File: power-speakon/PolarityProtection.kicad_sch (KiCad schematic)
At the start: 7 parts, among them Q201 BSC010N04LS, Q202 BSC010N04LS, U201 LM74502-Q1

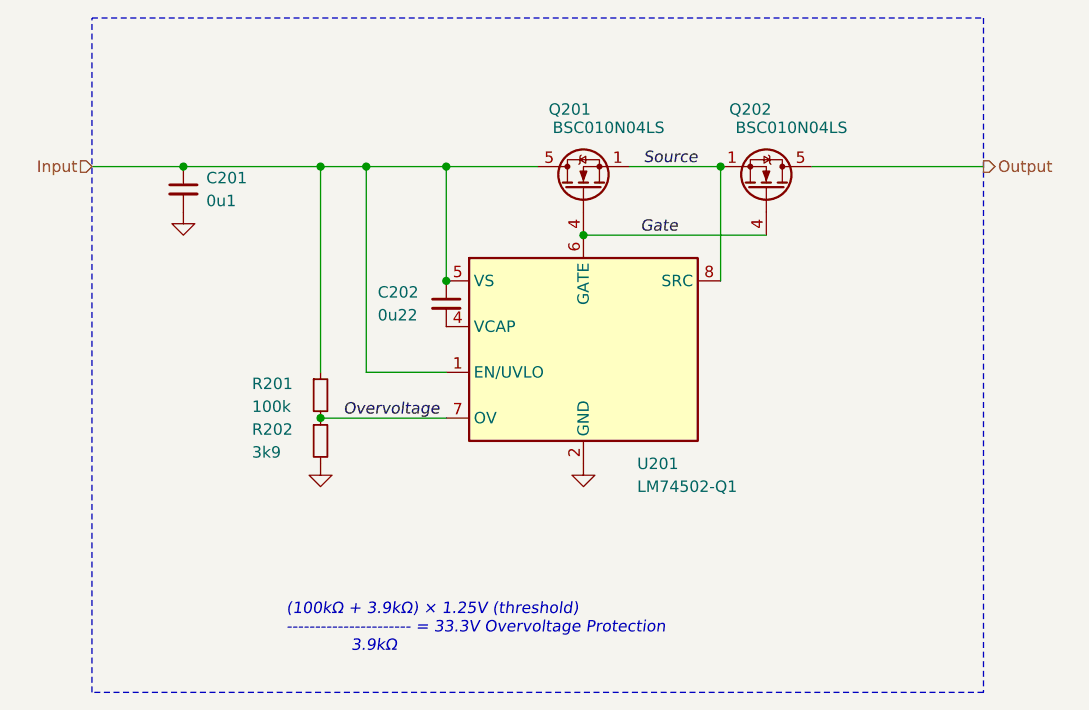
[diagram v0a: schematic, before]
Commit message: Update power symbols
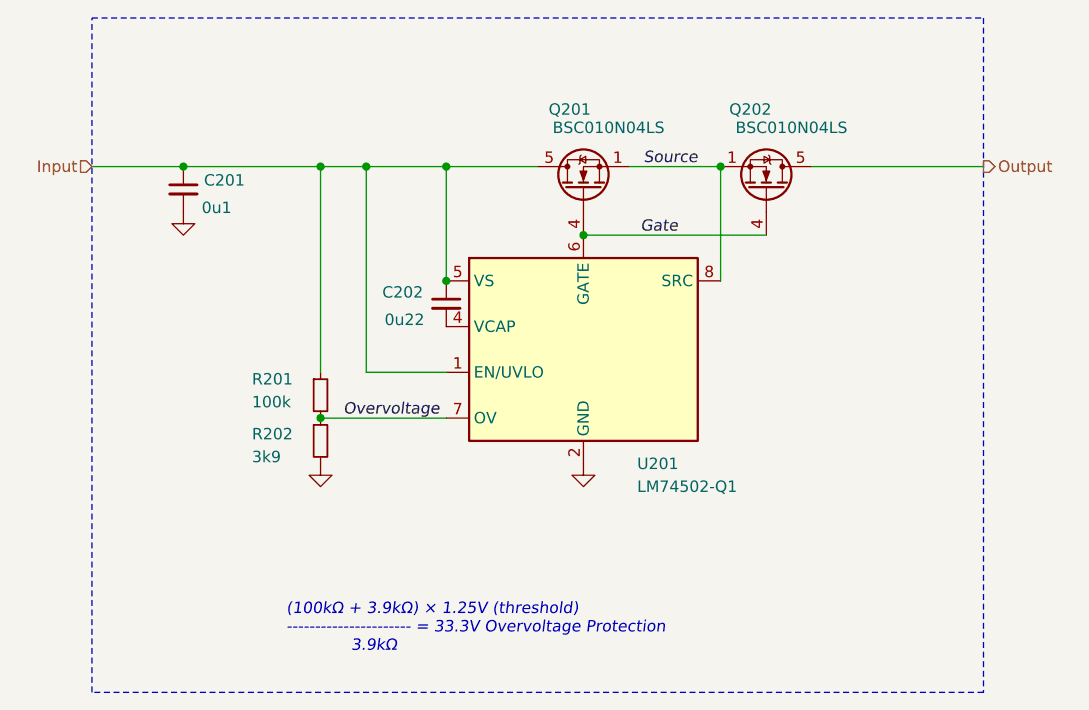
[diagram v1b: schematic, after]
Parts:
- C201: footprint Capacitor_SMD:C_0603_1608Metric -> V2_Capacitor_SMD:C_0603; symbol Device:C_Small -> V2_Device:C_0603_0u1; Mouser (none) -> 810-CGA3E2X7R1H104MA
- C202: footprint Capacitor_SMD:C_0603_1608Metric -> V2_Capacitor_SMD:C_0603; symbol Device:C_Small -> V2_Device:C_0603_0u22; Mouser (none) -> 603-CC0603JRX79BB224
- Q201, Q202: Mouser (none) -> 726-BSC010N04LS
- R201: footprint Resistor_SMD:R_0603_1608Metric -> V2_Resistor_SMD:R_0603; symbol Device:R_Small -> V2_Device:R_0603_100k; Mouser (none) -> 71-CRCW0603100KFKEAC
- R202: footprint Resistor_SMD:R_0603_1608Metric -> V2_Resistor_SMD:R_0603; symbol Device:R_Small -> V2_Device:R_0603_3k9; Mouser (none) -> 71-CRCW06033K90FKEAC
- U201: Mouser (none) -> 595-LM74502HQDDFRQ1
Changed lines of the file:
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@@
 	)
 	(symbol
-		(lib_id "power:GND")
+		(lib_id "V2_power:GND")
 		(at 111.76 91.44 0)
 		(unit 1)
@@
 		)
 		(property "Description" "Power symbol creates a global label with name \"GND\" , ground"
-			(at 111.76 91.44 0)
+			(at 111.506 101.854 0)
 			(effects
 				(font
@@
 			)
 		)
+		(property "Mouser" "726-BSC010N04LS"
+			(at 171.958 88.9 0)
+			(effects
+				(font
+					(size 1.27 1.27)
+				)
+				(hide yes)
+			)
+		)
 		(pin "1"
 		)
@@
 			)
 		)
+		(property "Mouser" "595-LM74502HQDDFRQ1"
+			(at 156.21 106.68 0)
+			(effects
+				(font
+					(size 1.27 1.27)
+				)
+				(hide yes)
+			)
+		)
 		(pin "1"
 		)
@@
 	)
 	(symbol
-		(lib_id "Device:R_Small")
+		(lib_id "V2_Device:R_0603_100k")
 		(at 127 111.76 0)
 		(unit 1)
@@
 		(dnp no)
 		(property "Reference" "R201"
-			(at 119.38 110.49 0)
+			(at 119.38 109.982 0)
 			(effects
 				(font
@@
 		)
 		(property "Value" "100k"
-			(at 119.38 113.03 0)
-			(effects
-				(font
-					(size 1.27 1.27)
-				)
-				(justify left)
-			)
-		)
-		(property "Footprint" "Resistor_SMD:R_0603_1608Metric"
+			(at 119.38 112.522 0)
+			(effects
+				(font
+					(size 1.27 1.27)
+				)
+				(justify left)
+			)
+		)
+		(property "Footprint" "V2_Resistor_SMD:R_0603"
 			(at 127 111.76 0)
 			(effects
@@
 			)
 		)
-		(property "Datasheet" "~"
+		(property "Datasheet" ""
 			(at 127 111.76 0)
 			(effects
@@
 			)
 		)
+		(property "Mouser" "71-CRCW0603100KFKEAC"
+			(at 127 127.254 0)
+			(effects
+				(font
+					(size 1.27 1.27)
+				)
+				(hide yes)
+			)
+		)
 		(pin "1"
 		)
@@
 	)
 	(symbol
-		(lib_id "Device:C_Small")
+		(lib_id "V2_Device:C_0603_0u1")
 		(at 111.76 88.9 0)
 		(unit 1)
@@
 		(dnp no)
 		(property "Reference" "C201"
-			(at 114.3 87.63 0)
+			(at 114.046 87.884 0)
 			(effects
 				(font
@@
 		)
 		(property "Value" "0u1"
-			(at 114.3 90.17 0)
-			(effects
-				(font
-					(size 1.27 1.27)
-				)
-				(justify left)
-			)
-		)
-		(property "Footprint" "Capacitor_SMD:C_0603_1608Metric"
+			(at 113.792 90.932 0)
+			(effects
+				(font
+					(size 1.27 1.27)
+				)
+				(justify left)
+			)
+		)
+		(property "Footprint" "V2_Capacitor_SMD:C_0603"
+			(at 111.76 105.918 0)
+			(effects
+				(font
+					(size 1.27 1.27)
+				)
+				(hide yes)
+			)
+		)
+		(property "Datasheet" ""
 			(at 111.76 88.9 0)
 			(effects
@@
 			)
 		)
-		(property "Datasheet" "~"
-			(at 111.76 88.9 0)
-			(effects
-				(font
-					(size 1.27 1.27)
-				)
-				(hide yes)
-			)
-		)
 		(property "Description" "Unpolarized capacitor, small symbol"
-			(at 111.76 88.9 0)
+			(at 111.76 102.362 0)
+			(effects
+				(font
+					(size 1.27 1.27)
+				)
+				(hide yes)
+			)
+		)
+		(property "Mouser" "810-CGA3E2X7R1H104MA"
+			(at 111.76 105.918 0)
 			(effects
 				(font
@@
 	)
 	(symbol
-		(lib_id "Device:C_Small")
+		(lib_id "V2_Device:C_0603_0u22")
 		(at 140.97 101.6 0)
 		(unit 1)
@@
 		(dnp no)
 		(property "Reference" "C202"
-			(at 133.35 100.33 0)
+			(at 133.858 100.33 0)
 			(effects
 				(font
@@
 		)
 		(property "Value" "0u22"
-			(at 133.35 102.87 0)
-			(effects
-				(font
-					(size 1.27 1.27)
-				)
-				(justify left)
-			)
-		)
-		(property "Footprint" "Capacitor_SMD:C_0603_1608Metric"
+			(at 134.112 103.378 0)
+			(effects
+				(font
+					(size 1.27 1.27)
+				)
+				(justify left)
+			)
+		)
+		(property "Footprint" "V2_Capacitor_SMD:C_0603"
+			(at 140.97 118.618 0)
+			(effects
+				(font
+					(size 1.27 1.27)
+				)
+				(hide yes)
+			)
+		)
+		(property "Datasheet" ""
 			(at 140.97 101.6 0)
 			(effects
@@
 			)
 		)
-		(property "Datasheet" "~"
-			(at 140.97 101.6 0)
-			(effects
-				(font
-					(size 1.27 1.27)
-				)
-				(hide yes)
-			)
-		)
 		(property "Description" "Unpolarized capacitor, small symbol"
-			(at 140.97 101.6 0)
+			(at 140.97 115.062 0)
+			(effects
+				(font
+					(size 1.27 1.27)
+				)
+				(hide yes)
+			)
+		)
+		(property "Mouser" "603-CC0603JRX79BB224"
+			(at 140.97 118.618 0)
 			(effects
 				(font
@@
 	)
 	(symbol
-		(lib_id "Device:R_Small")
+		(lib_id "V2_Device:R_0603_3k9")
 		(at 127 116.84 0)
 		(unit 1)
@@
 		(dnp no)
 		(property "Reference" "R202"
-			(at 119.38 115.57 0)
+			(at 119.38 116.078 0)
 			(effects
 				(font
@@
 		)
 		(property "Value" "3k9"
-			(at 119.38 118.11 0)
-			(effects
-				(font
-					(size 1.27 1.27)
-				)
-				(justify left)
-			)
-		)
-		(property "Footprint" "Resistor_SMD:R_0603_1608Metric"
+			(at 119.38 118.618 0)
+			(effects
+				(font
+					(size 1.27 1.27)
+				)
+				(justify left)
+			)
+		)
+		(property "Footprint" "V2_Resistor_SMD:R_0603"
 			(at 127 116.84 0)
 			(effects
@@
 			)
 		)
-		(property "Datasheet" "~"
+		(property "Datasheet" ""
 			(at 127 116.84 0)
 			(effects
@@
 		(property "Description" "Resistor, small symbol"
 			(at 127 116.84 0)
+			(effects
+				(font
+					(size 1.27 1.27)
+				)
+				(hide yes)
+			)
+		)
+		(property "Mouser" "71-CRCW06033K90FKEAC"
+			(at 127 132.334 0)
 			(effects
 				(font
@@
 			)
 		)
+		(property "Mouser" "726-BSC010N04LS"
+			(at 160.782 88.9 0)
+			(effects
+				(font
+					(size 1.27 1.27)
+				)
+				(hide yes)
+			)
+		)
 		(pin "1"
 		)
@@
 	)
 	(symbol
-		(lib_id "power:GND")
+		(lib_id "V2_power:GND")
 		(at 156.21 119.38 0)
 		(unit 1)
@@
 		)
 		(property "Description" "Power symbol creates a global label with name \"GND\" , ground"
-			(at 156.21 119.38 0)
+			(at 155.956 129.794 0)
 			(effects
 				(font
@@
 	)
 	(symbol
-		(lib_id "power:GND")
+		(lib_id "V2_power:GND")
 		(at 127 119.38 0)
 		(unit 1)
@@
 		)
 		(property "Description" "Power symbol creates a global label with name \"GND\" , ground"
-			(at 127 119.38 0)
-			(effects
-				(font
+			(at 126.746 129.794 0)
+			(effects
+				(font

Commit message: Update parts
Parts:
- C201: Manufacturer (none) -> TDK; Product (none) -> CGA3E2X7R1H104M080AA
- C202: Manufacturer (none) -> YAGEO; Product (none) -> CC0603JRX7R9BB224
- Q201, Q202: Manufacturer (none) -> Infineon Technologies; Product (none) -> BSC010N04LS
- R201: Manufacturer (none) -> Vishay; Product (none) -> CRCW0603100KFKEAC; Rating (none) -> 100mW
- R202: Manufacturer (none) -> Vishay; Product (none) -> CRCW06033K90FKEAC; Rating (none) -> 100mW
- U201: Manufacturer (none) -> Texas Instruments; Product (none) -> LM74502HQDDFRQ1
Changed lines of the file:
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@@
+			)
+		)
+		(property "Product" "BSC010N04LS"
+			(at 176.53 88.9 0)
+			(effects
+				(font
+					(size 1.27 1.27)
+				)
+				(hide yes)
+			)
+		)
+		(property "Manufacturer" "Infineon Technologies"
+			(at 173.99 88.9 0)
+			(effects
+				(font
+					(size 1.27 1.27)
+				)
+				(hide yes)
+			)
+		)
+		(property "Sim.Enable" ""
+			(at 156.21 88.9 90)
+			(effects
+				(font
+					(size 1.27 1.27)
+				)
+				(hide yes)
 			)
 		)
@@
 			)
 		)
+		(property "Product" "LM74502HQDDFRQ1"
+			(at 156.21 144.78 0)
+			(effects
+				(font
+					(size 1.27 1.27)
+				)
+				(hide yes)
+			)
+		)
+		(property "Manufacturer" "Texas Instruments"
+			(at 156.21 142.24 0)
+			(effects
+				(font
+					(size 1.27 1.27)
+				)
+				(hide yes)
+			)
+		)
+		(property "Sim.Enable" ""
+			(at 156.21 106.68 0)
+			(effects
+				(font
+					(size 1.27 1.27)
+				)
+				(hide yes)
+			)
+		)
 		(pin "1"
 		)
@@
 			)
 		)
+		(property "Rating" "100mW"
+			(at 127 132.08 0)
+			(effects
+				(font
+					(size 1.27 1.27)
+				)
+				(hide yes)
+			)
+		)
+		(property "Manufacturer" "Vishay"
+			(at 127 127 0)
+			(effects
+				(font
+					(size 1.27 1.27)
+				)
+				(hide yes)
+			)
+		)
+		(property "Product" "CRCW0603100KFKEAC"
+			(at 127 129.54 0)
+			(effects
+				(font
+					(size 1.27 1.27)
+				)
+				(hide yes)
+			)
+		)
+		(property "Sim.Enable" ""
+			(at 127 111.76 0)
+			(effects
+				(font
+					(size 1.27 1.27)
+				)
+				(hide yes)
+			)
+		)
 		(pin "1"
 		)
@@
 			)
 		)
+		(property "Manufacturer" "TDK"
+			(at 111.76 104.14 0)
+			(effects
+				(font
+					(size 1.27 1.27)
+				)
+				(hide yes)
+			)
+		)
+		(property "Product" "CGA3E2X7R1H104M080AA"
+			(at 111.76 106.68 0)
+			(effects
+				(font
+					(size 1.27 1.27)
+				)
+				(hide yes)
+			)
+		)
+		(property "Sim.Enable" ""
+			(at 111.76 88.9 0)
+			(effects
+				(font
+					(size 1.27 1.27)
+				)
+				(hide yes)
+			)
+		)
 		(pin "1"
 		)
@@
 			)
 		)
+		(property "Product" "CC0603JRX7R9BB224"
+			(at 140.97 119.38 0)
+			(effects
+				(font
+					(size 1.27 1.27)
+				)
+				(hide yes)
+			)
+		)
+		(property "Manufacturer" "YAGEO"
+			(at 140.97 116.84 0)
+			(effects
+				(font
+					(size 1.27 1.27)
+				)
+				(hide yes)
+			)
+		)
+		(property "Sim.Enable" ""
+			(at 140.97 101.6 0)
+			(effects
+				(font
+					(size 1.27 1.27)
+				)
+				(hide yes)
+			)
+		)
 		(pin "1"
 		)
@@
 		(property "Mouser" "71-CRCW06033K90FKEAC"
 			(at 127 132.334 0)
+			(effects
+				(font
+					(size 1.27 1.27)
+				)
+				(hide yes)
+			)
+		)
+		(property "Product" "CRCW06033K90FKEAC"
+			(at 127 134.62 0)
+			(effects
+				(font
+					(size 1.27 1.27)
+				)
+				(hide yes)
+			)
+		)
+		(property "Manufacturer" "Vishay"
+			(at 127 132.08 0)
+			(effects
+				(font
+					(size 1.27 1.27)
+				)
+				(hide yes)
+			)
+		)
+		(property "Rating" "100mW"
+			(at 127 137.16 0)
+			(effects
+				(font
+					(size 1.27 1.27)
+				)
+				(hide yes)
+			)
+		)
+		(property "Sim.Enable" ""
+			(at 127 116.84 0)
 			(effects
 				(font
@@
 			(effects
 				(font
+					(size 1.27 1.27)
+				)
+				(hide yes)
+			)
+		)
+		(property "Product" "BSC010N04LS"
+			(at 156.21 88.9 0)
+			(effects
+				(font
+					(size 1.27 1.27)
+				)
+				(hide yes)
+			)
+		)
+		(property "Manufacturer" "Infineon Technologies"
+			(at 158.75 88.9 0)
+			(effects
+				(font
+					(size 1.27 1.27)
+				)
+				(hide yes)
+			)
+		)
+		(property "Sim.Enable" ""
+			(at 176.53 88.9 90)
+			(effects
+				(font

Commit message: Refresh
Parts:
- C201: Rating (none) -> 50V
- Q201, Q202: Polarity (none) -> N; Rating (none) -> 40V
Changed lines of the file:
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@@
 			)
 		)
-		(property "Sim.Enable" ""
-			(at 156.21 88.9 90)
+		(property "Rating" "40V"
+			(at 176.53 88.9 0)
+			(effects
+				(font
+					(size 1.27 1.27)
+				)
+				(hide yes)
+			)
+		)
+		(property "Polarity" "N"
+			(at 173.99 88.9 0)
 			(effects
 				(font
@@
 			)
 		)
-		(property "Sim.Enable" ""
-			(at 156.21 106.68 0)
-			(effects
-				(font
-					(size 1.27 1.27)
-				)
-				(hide yes)
-			)
-		)
 		(pin "1"
 		)
@@
 			)
 		)
-		(property "Sim.Enable" ""
-			(at 127 111.76 0)
-			(effects
-				(font
-					(size 1.27 1.27)
-				)
-				(hide yes)
-			)
-		)
 		(pin "1"
 		)
@@
 			)
 		)
-		(property "Sim.Enable" ""
-			(at 111.76 88.9 0)
+		(property "Rating" "50V"
+			(at 111.76 111.76 0)
 			(effects
 				(font
@@
 			)
 		)
-		(property "Sim.Enable" ""
-			(at 140.97 101.6 0)
-			(effects
-				(font
-					(size 1.27 1.27)
-				)
-				(hide yes)
-			)
-		)
 		(pin "1"
 		)
@@
 		(property "Rating" "100mW"
 			(at 127 137.16 0)
-			(effects
-				(font
-					(size 1.27 1.27)
-				)
-				(hide yes)
-			)
-		)
-		(property "Sim.Enable" ""
-			(at 127 116.84 0)
 			(effects
 				(font
@@
 			)
 		)
-		(property "Sim.Enable" ""
-			(at 176.53 88.9 90)
-			(effects
-				(font
+		(property "Rating" "40V"
+			(at 156.21 88.9 0)
+			(effects
+				(font
+					(size 1.27 1.27)
+				)
+				(hide yes)
+			)
+		)
+		(property "Polarity" "N"
+			(at 158.75 88.9 0)
+			(effects
+				(font

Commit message: Use date as revision
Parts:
- U201: Mouser 595-LM74502HQDDFRQ1 -> 595-LM74502QDDFRQ1; Product LM74502HQDDFRQ1 -> LM74502QDDFRQ1
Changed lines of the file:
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@@
 			)
 		)
-		(property "Mouser" "595-LM74502HQDDFRQ1"
+		(property "Mouser" "595-LM74502QDDFRQ1"
 			(at 156.21 106.68 0)
 			(effects
@@
 			)
 		)
-		(property "Product" "LM74502HQDDFRQ1"
+		(property "Product" "LM74502QDDFRQ1"
 			(at 156.21 144.78 0)
 			(effects

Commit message: Update Library
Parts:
- C201: symbol V2_Device:C_0603_0u1 -> V2_Capacitor:0603_0u1
- C202: symbol V2_Device:C_0603_0u22 -> V2_Capacitor:0603_0u22
- R201: symbol V2_Device:R_0603_100k -> V2_Resistor:0603_100k
- R202: symbol V2_Device:R_0603_3k9 -> V2_Resistor:0603_3k9
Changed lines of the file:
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@@
 		(on_board yes)
 		(dnp no)
-		(property "Reference" "#PWR0201"
+		(property "Reference" "#PWR201"
 			(at 111.76 97.79 0)
 			(effects
@@
 			(project "power-speakon"
 				(path "/6c8448b4-b04d-47e1-934e-e40cbe27a7be/d58e122d-3dfd-484c-8dd2-db8f39216d59"
-					(reference "#PWR0201")
+					(reference "#PWR201")
 					(unit 1)
 				)
@@
 	)
 	(symbol
-		(lib_id "V2_Device:R_0603_100k")
+		(lib_id "V2_Resistor:0603_100k")
 		(at 127 111.76 0)
 		(unit 1)
@@
 	)
 	(symbol
-		(lib_id "V2_Device:C_0603_0u1")
+		(lib_id "V2_Capacitor:0603_0u1")
 		(at 111.76 88.9 0)
 		(unit 1)
@@
 	)
 	(symbol
-		(lib_id "V2_Device:C_0603_0u22")
+		(lib_id "V2_Capacitor:0603_0u22")
 		(at 140.97 101.6 0)
 		(unit 1)
@@
 	)
 	(symbol
-		(lib_id "V2_Device:R_0603_3k9")
+		(lib_id "V2_Resistor:0603_3k9")
 		(at 127 116.84 0)
 		(unit 1)
@@
 		(on_board yes)
 		(dnp no)
-		(property "Reference" "#PWR0203"
+		(property "Reference" "#PWR203"
 			(at 156.21 125.73 0)
 			(effects
@@
 			(project "power-speakon"
 				(path "/6c8448b4-b04d-47e1-934e-e40cbe27a7be/d58e122d-3dfd-484c-8dd2-db8f39216d59"
-					(reference "#PWR0203")
+					(reference "#PWR203")
 					(unit 1)
 				)
@@
 		(on_board yes)
 		(dnp no)
-		(property "Reference" "#PWR0202"
+		(property "Reference" "#PWR202"
 			(at 127 125.73 0)
 			(effects
@@
 			(project "power-speakon"
 				(path "/6c8448b4-b04d-47e1-934e-e40cbe27a7be/d58e122d-3dfd-484c-8dd2-db8f39216d59"
-					(reference "#PWR0202")
+					(reference "#PWR202")
 					(unit 1)
 				)

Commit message: Update
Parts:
- C201: Id (none) -> Capacitor:${SYMBOL_NAME}
- C202: Id (none) -> Capacitor:${SYMBOL_NAME}; Rating (none) -> 50V
- Q201, Q202: Id (none) -> MOSFET:${SYMBOL_NAME}
- R201, R202: Id (none) -> Resistor:${SYMBOL_NAME}
- U201: Id (none) -> PolarityProtection:${SYMBOL_NAME}; Rating (none) -> 60uA
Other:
- title: Polarity Protection -> V2 Power SpeakOn

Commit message: Good Bye Imperial
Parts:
- C201: footprint V2_Capacitor_SMD:C_0603 -> V2_Capacitor_SMD:C_1608; symbol V2_Capacitor:0603_0u1 -> V2_Capacitor:1608_0u1
- C202: footprint V2_Capacitor_SMD:C_0603 -> V2_Capacitor_SMD:C_1608; symbol V2_Capacitor:0603_0u22 -> V2_Capacitor:1608_0u22
- R201: footprint V2_Resistor_SMD:R_0603 -> V2_Resistor_SMD:R_1608; symbol V2_Resistor:0603_100k -> V2_Resistor:1608_100k
- R202: footprint V2_Resistor_SMD:R_0603 -> V2_Resistor_SMD:R_1608; symbol V2_Resistor:0603_3k9 -> V2_Resistor:1608_3k9
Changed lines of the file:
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@@
 	)
 	(symbol
-		(lib_id "V2_Resistor:0603_100k")
+		(lib_id "V2_Resistor:1608_100k")
 		(at 127 111.76 0)
 		(unit 1)
@@
 			)
 		)
-		(property "Footprint" "V2_Resistor_SMD:R_0603"
+		(property "Footprint" "V2_Resistor_SMD:R_1608"
 			(at 127 111.76 0)
 			(hide yes)
@@
 	)
 	(symbol
-		(lib_id "V2_Capacitor:0603_0u1")
+		(lib_id "V2_Capacitor:1608_0u1")
 		(at 111.76 88.9 0)
 		(unit 1)
@@
 			)
 		)
-		(property "Footprint" "V2_Capacitor_SMD:C_0603"
+		(property "Footprint" "V2_Capacitor_SMD:C_1608"
 			(at 111.76 105.918 0)
 			(hide yes)
@@
 	)
 	(symbol
-		(lib_id "V2_Capacitor:0603_0u22")
+		(lib_id "V2_Capacitor:1608_0u22")
 		(at 140.97 101.6 0)
 		(unit 1)
@@
 			)
 		)
-		(property "Footprint" "V2_Capacitor_SMD:C_0603"
+		(property "Footprint" "V2_Capacitor_SMD:C_1608"
 			(at 140.97 118.618 0)
 			(hide yes)
@@
 	)
 	(symbol
-		(lib_id "V2_Resistor:0603_3k9")
+		(lib_id "V2_Resistor:1608_3k9")
 		(at 127 116.84 0)
 		(unit 1)
@@
 			)
 		)
-		(property "Footprint" "V2_Resistor_SMD:R_0603"
+		(property "Footprint" "V2_Resistor_SMD:R_1608"
 			(at 127 116.84 0)
 			(hide yes)
